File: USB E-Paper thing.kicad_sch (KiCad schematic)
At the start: 53 parts, among them J3 EXTRA2, J4 DOWNSTREAM, J5 SWD, J9 SPI, Q1 AO3400A, SW1 BUTTON0, SW2 BUTTON1, SW3 BUTTON2, SW4 BUTTON3, U1 STM32L151C8TxA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

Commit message: WIP
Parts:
- C1, C2: value 8pF -> 20pF; LCSC C1578 -> C1554
- J3, J4, J9: now not fitted; now left out of the parts list
- J5: now left out of the parts list
- R14: footprint Resistor_SMD:R_0402_1005Metric -> Resistor_SMD:R_0603_1608Metric
- R2: value 27 -> 33
- R5: value 68 -> 50
- Y1: value 24 MHz -> 12 MHz; footprint Crystal:Crystal_SMD_2520-4Pin_2.5x2.0mm -> Crystal:Crystal_SMD_3225-4Pin_3.2x2.5mm; LCSC C284163 -> C9002

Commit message: Use single FPC connector for debug signals and downstream
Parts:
- removed J4: DOWNSTREAM, Connector_PinHeader_2.54mm:PinHeader_1x04_P2.54mm_Horizontal, symbol Connector:Conn_01x04_Pin
- removed J9: SPI, Connector_JST:JST_PH_B6B-PH-K_1x06_P2.00mm_Vertical, symbol Connector_Generic:Conn_01x06
- J3: footprint Connector_PinHeader_2.54mm:PinHeader_1x08_P2.54mm_Vertical -> local:FPC_14; symbol Connector:Conn_01x08_Pin -> Connector:Conn_01x14_Pin; LCSC (none) -> C262682; now fitted; now in the parts list
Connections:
- net BUSY_DBG: now also J3.12 (Pin_12)
- net D/~{C}: now also J3.13 (Pin_13)
- net GND: now also J3.2 (Pin_2); no longer J3.8 (Pin_8)
- net MOSI: now also J3.10 (Pin_10)
- net PA15: no longer J3.7 (Pin_7)
- net PB4: no longer J3.6 (Pin_6)
- net PB6: now also J3.6 (Pin_6); no longer J3.4 (Pin_4)
- net PB7: now also J3.7 (Pin_7); no longer J3.3 (Pin_3)
- net PB8: now also J3.8 (Pin_8); no longer J3.2 (Pin_2)
- net SCLK: now also J3.11 (Pin_11)
- net SERIAL_RX: now also J3.3 (Pin_3)
- net SERIAL_TX: now also J3.4 (Pin_4)
- net ~{CS}: now also J3.9 (Pin_9)
- net ~{RES}: now also J3.14 (Pin_14)

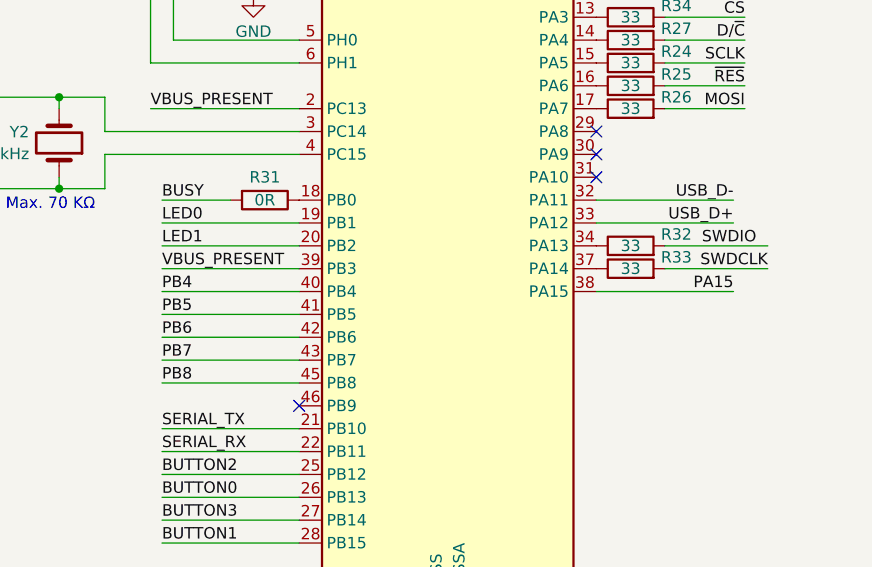
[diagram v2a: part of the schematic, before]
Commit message: switch to JLCPCB version of USBC connect fp
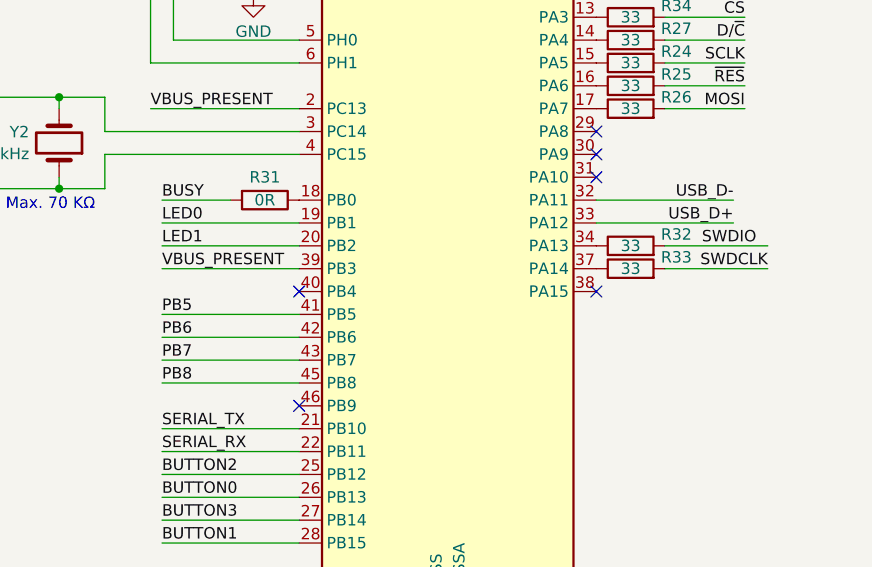
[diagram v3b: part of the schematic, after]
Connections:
- net PA15: no longer names the net of U1.38 (PA15)
- net PB4: no longer names the net of U1.40 (PB4)
- no-connect marks 5 -> 7
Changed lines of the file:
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@@
   )
   (no_connect (at 247.65 93.98))
+  (no_connect (at 214.63 109.22))
   (no_connect (at 247.65 91.44))
   (no_connect (at 214.63 121.92))
   (no_connect (at 237.49 30.48))
+  (no_connect (at 247.65 109.22))
   (no_connect (at 247.65 96.52))
   (wire (pts (xy 256.54 29.21) (xy 273.05 29.21))
@@
     (stroke (width 0) (type default))
   )
-  (wire (pts (xy 199.39 109.22) (xy 214.63 109.22))
-    (stroke (width 0) (type default))
-  )
   (wire (pts (xy 128.27 88.9) (xy 132.08 88.9))
     (stroke (width 0) (type default))
@@
   )
   (wire (pts (xy 52.07 153.67) (xy 60.96 153.67))
-    (stroke (width 0) (type default))
-  )
-  (wire (pts (xy 247.65 109.22) (xy 262.89 109.22))
     (stroke (width 0) (type default))
   )
@@
     (effects (font (size 1.27 1.27)) (justify left bottom))
   )
-  (label "PA15" (at 262.89 109.22 180) (fields_autoplaced)
-    (effects (font (size 1.27 1.27)) (justify right bottom))
-  )
   (label "LED0" (at 101.6 25.4 0) (fields_autoplaced)
     (effects (font (size 1.27 1.27)) (justify left bottom))
@@
     (effects (font (size 1.27 1.27)) (justify left bottom))
   )
-  (label "PB4" (at 199.39 109.22 0) (fields_autoplaced)
-    (effects (font (size 1.27 1.27)) (justify left bottom))
-  )

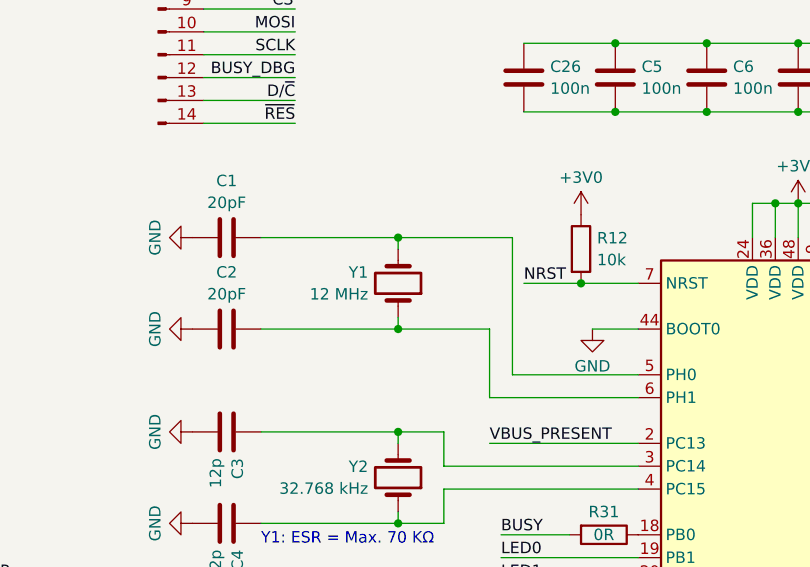
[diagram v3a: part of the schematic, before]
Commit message: Fix all DRC violations, fix 12 MHz crystal connections
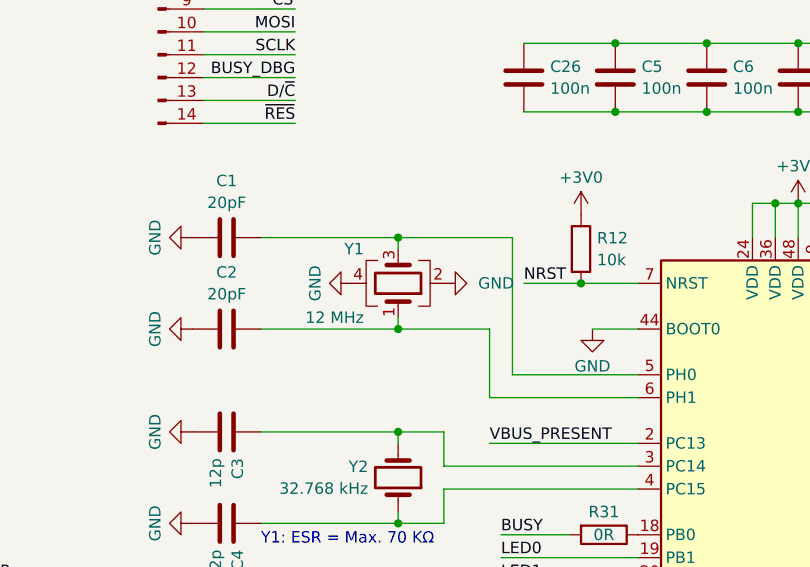
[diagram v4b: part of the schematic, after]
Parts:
- Y1: symbol local:Crystal_4pin -> Device:Crystal_GND24
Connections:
- net GND: now also Y1.2, Y1.4
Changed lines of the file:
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@@
     )
   )
-  (symbol (lib_id "local:Crystal_4pin") (at 187.96 71.12 270) (mirror x) (unit 1)
+  (symbol (lib_id "Device:Crystal_GND24") (at 187.96 71.12 270) (mirror x) (unit 1)
     (in_bom yes) (on_board yes) (dnp no)
-    (property "Reference" "Y1" (at 184.6326 69.9079 90)
-      (effects (font (size 1.27 1.27)) (justify right))
-    )
-    (property "Value" "12 MHz" (at 184.6326 72.3321 90)
+    (property "Reference" "Y1" (at 184.15 67.31 90)
+      (effects (font (size 1.27 1.27)) (justify right))
+    )
+    (property "Value" "12 MHz" (at 184.15 74.93 90)
       (effects (font (size 1.27 1.27)) (justify right))
     )
@@
     )
   )
+  (symbol (lib_id "power:GND") (at 193.04 71.12 90) (unit 1)
+    (in_bom yes) (on_board yes) (dnp no) (fields_autoplaced)
+    (property "Reference" "#PWR03" (at 199.39 71.12 0)
+      (effects (font (size 1.27 1.27)) hide)
+    )
+    (property "Value" "GND" (at 196.85 71.12 90)
+      (effects (font (size 1.27 1.27)) (justify right))
+    )
+    (property "Footprint" "" (at 193.04 71.12 0)
+      (effects (font (size 1.27 1.27)) hide)
+    )
+    (property "Datasheet" "" (at 193.04 71.12 0)
+      (effects (font (size 1.27 1.27)) hide)
+    )
+    (pin "1")
+    (instances
+      (project "USB E-Paper thing"
+        (path "/03659e82-b7b8-4d3e-8633-26f17364684b"
+          (reference "#PWR03") (unit 1)
+        )
+      )
+    )
+  )
   (symbol (lib_id "Switch:SW_Push") (at 114.3 71.12 90) (mirror x) (unit 1)
     (in_bom yes) (on_board yes) (dnp no)
@@
         )
       )
+    )
+  )
+  (symbol (lib_id "power:GND") (at 182.88 71.12 270) (unit 1)
+    (in_bom yes) (on_board yes) (dnp no) (fields_autoplaced)
+    (property "Reference" "#PWR02" (at 176.53 71.12 0)
+      (effects (font (size 1.27 1.27)) hide)
+    )
+    (property "Value" "GND" (at 178.7469 71.12 0)
+      (effects (font (size 1.27 1.27)))
+    )
+    (property "Footprint" "" (at 182.88 71.12 0)
+      (effects (font (size 1.27 1.27)) hide)
+    )
+    (property "Datasheet" "" (at 182.88 71.12 0)
+      (effects (font (size 1.27 1.27)) hide)
+    )
+    (pin "1")
+    (instances
+      (project "USB E-Paper thing"
+        (path "/03659e82-b7b8-4d3e-8633-26f17364684b"
+          (reference "#PWR02") (unit 1)
+        )
+      )
